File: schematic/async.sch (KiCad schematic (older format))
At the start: 79 parts, among them J1 LOAD, J2 Solar panel, J3 Battery, J4 Screw_Terminal_01x03, J5 Temperature, J6 SD_Micro_5V, J7 Screw_Terminal_01x03, Q1 IRF4905, Q2 IRF4905, Q3 IRF4905, Q4 2N3904, Q5 2N3904, Q6 IRF4905, Q7 2N3904, Q8 IRF4905, Q9 2N3904, SW1 Backlight control, T1 Mains Transformer, U1 ACS712module, U10 ATMEGA328-PU, U2 IR2110, U3 IR2110, U4 DS18B20, U5 ACS712module, U6 DS18B20, U7 DS1307_RTC, U8 MP2307_DC-DC_module, U9 LCDSerial2004

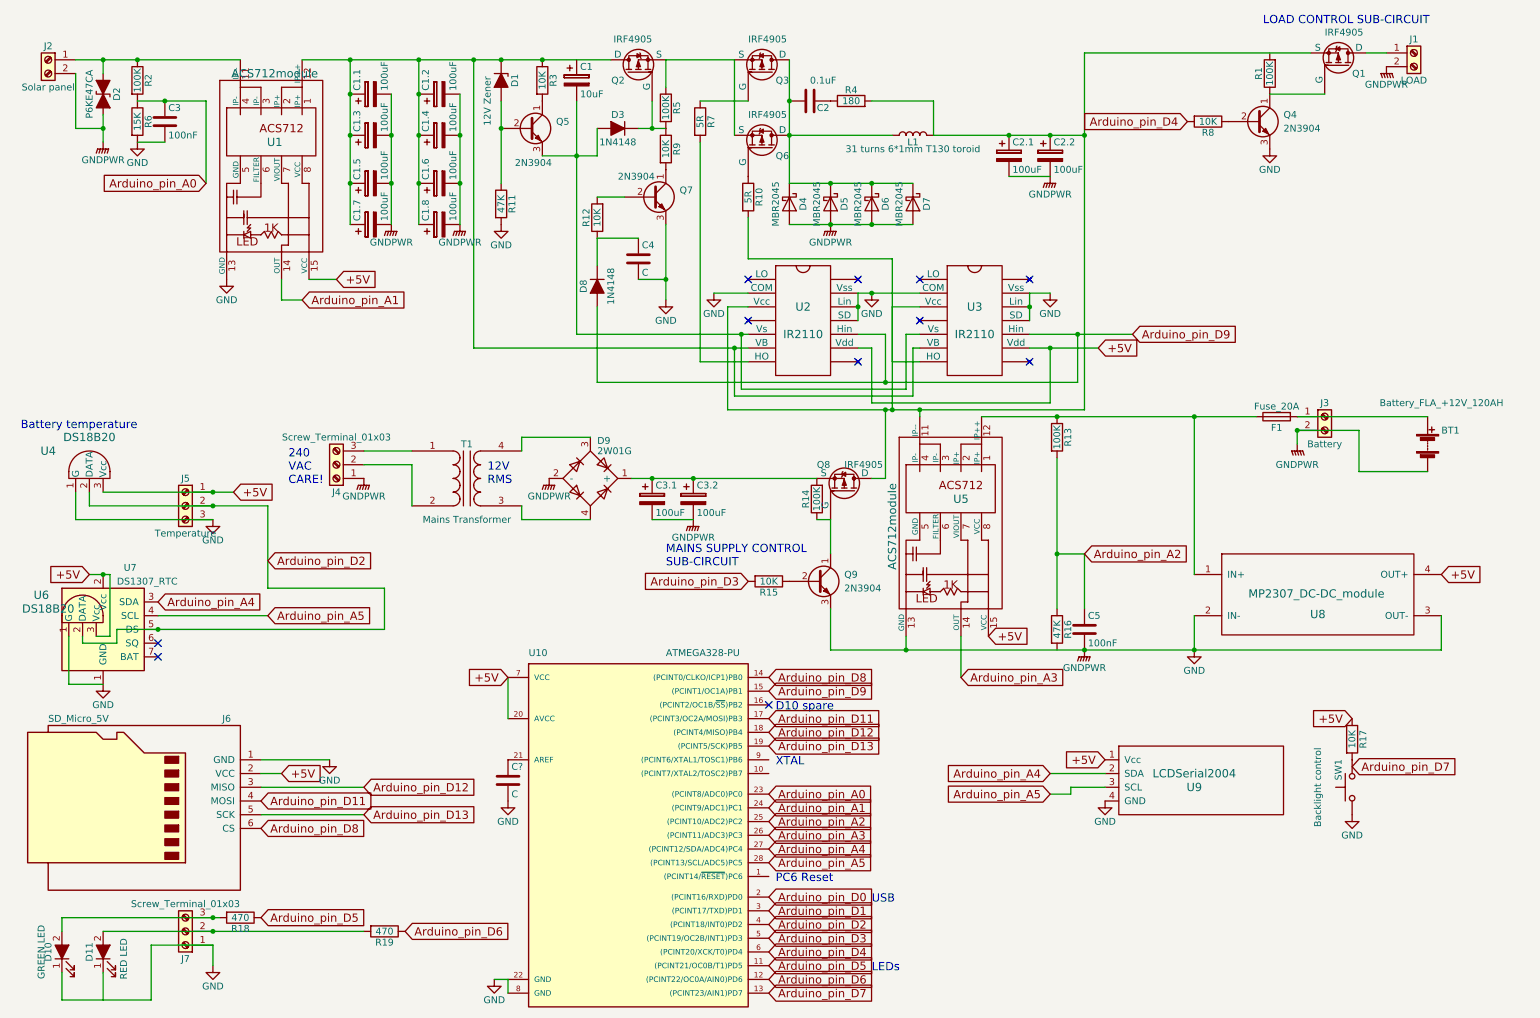
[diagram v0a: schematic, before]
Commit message: added reset button
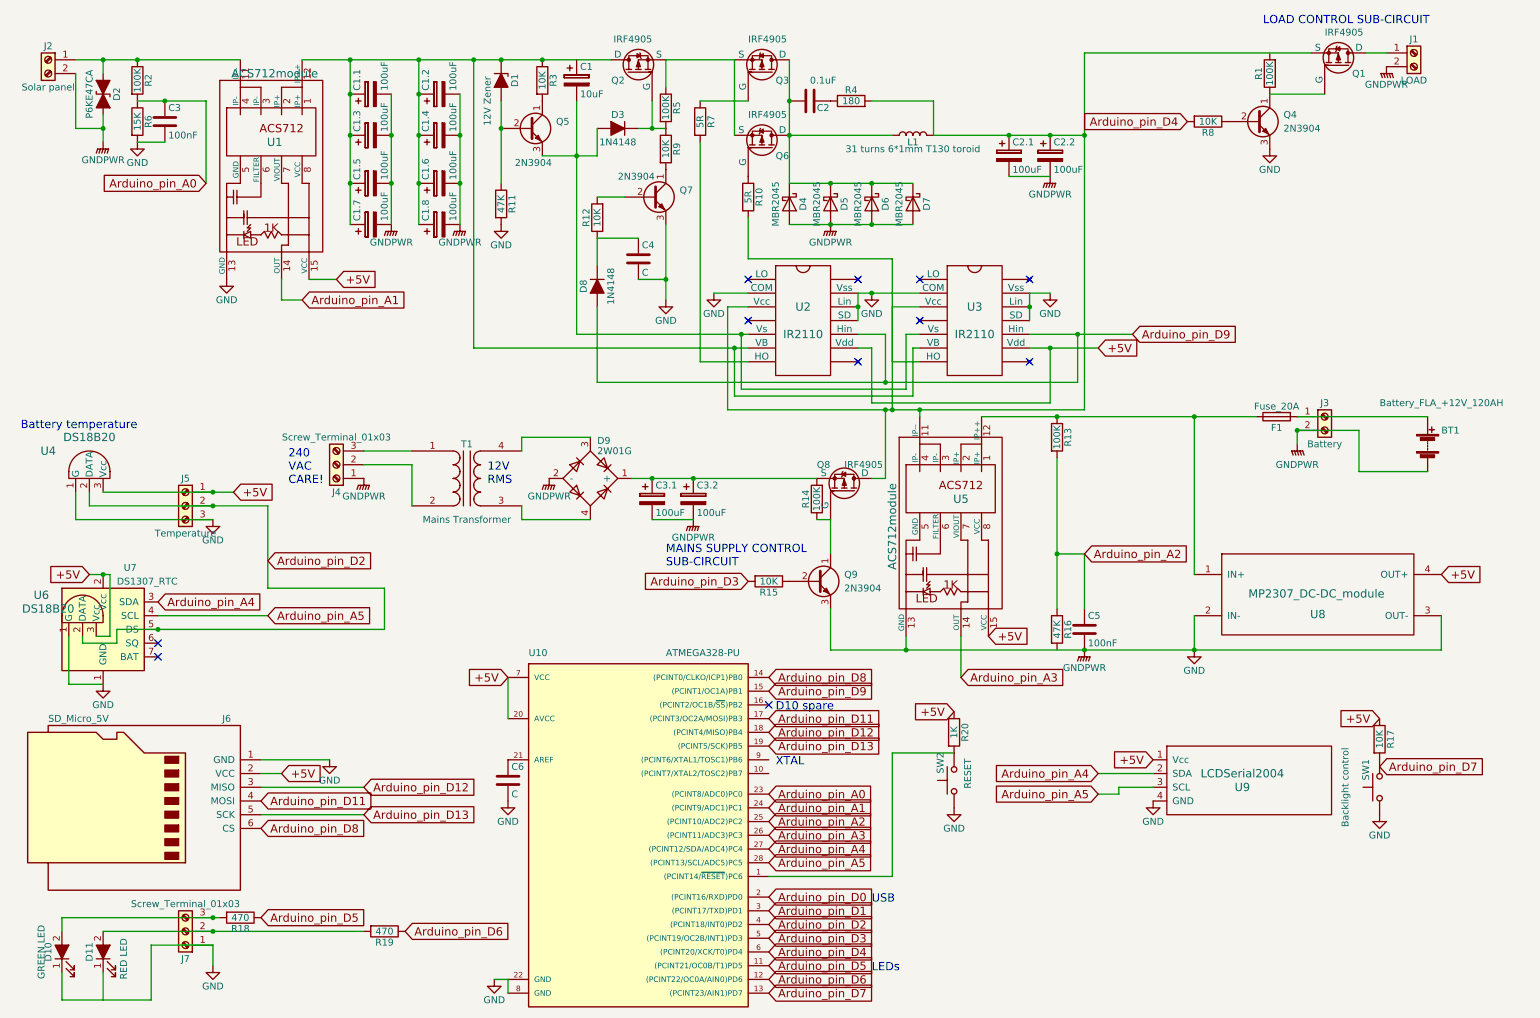
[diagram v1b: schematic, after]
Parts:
- added R20: 1K, symbol R
- added SW2: RESET, symbol SW_Push
- gave numbers to parts that had none: 1
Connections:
- net +5V: now also R20.1
- net GND: now also SW2.1
- net at U10.1 ((PCINT14/~RESET~)PC6): now also R20.2, SW2.2
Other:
- note removed: "PC6 Reset"
- moved on the sheet: R17, SW1, U9
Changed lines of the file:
@@
 L LCDSerial2004 U9
 U 1 1 5AF66609
-P 9050 6150
-F 0 "U9" H 9050 6150 60  0000 C CNN
-F 1 "LCDSerial2004" H 9050 6250 60  0000 C CNN
-F 2 "" H 9050 6150 60  0001 C CNN
-F 3 "" H 9050 6150 60  0001 C CNN
-	1    9050 6150
-	1    0    0    -1
-$EndComp
-Text GLabel 8400 5950 0    60   Input ~ 0
+P 9400 6150
+F 0 "U9" H 9400 6150 60  0000 C CNN
+F 1 "LCDSerial2004" H 9400 6250 60  0000 C CNN
+F 2 "" H 9400 6150 60  0001 C CNN
+F 3 "" H 9400 6150 60  0001 C CNN
+	1    9400 6150
+	1    0    0    -1
+$EndComp
+Text GLabel 8750 5950 0    60   Input ~ 0
 +5V
 $Comp
-L GND #PWR24
+L GND #PWR25
 U 1 1 5AF6660A
-P 8400 6250
-F 0 "#PWR24" H 8400 6000 50  0001 C CNN
-F 1 "GND" H 8400 6100 50  0000 C CNN
-F 2 "" H 8400 6250 50  0001 C CNN
-F 3 "" H 8400 6250 50  0001 C CNN
-	1    8400 6250
-	1    0    0    -1
-$EndComp
-Text GLabel 8000 6050 0    60   Input ~ 0
+P 8750 6250
+F 0 "#PWR25" H 8750 6000 50  0001 C CNN
+F 1 "GND" H 8750 6100 50  0000 C CNN
+F 2 "" H 8750 6250 50  0001 C CNN
+F 3 "" H 8750 6250 50  0001 C CNN
+	1    8750 6250
+	1    0    0    -1
+$EndComp
+Text GLabel 8350 6050 0    60   Input ~ 0
 Arduino_pin_A4
 Wire Wire Line
-	8000 6050 8400 6050
-Text GLabel 8000 6200 0    60   Input ~ 0
+	8350 6050 8750 6050
+Text GLabel 8350 6200 0    60   Input ~ 0
 Arduino_pin_A5
 Wire Wire Line
-	8000 6200 8150 6200
-Wire Wire Line
-	8150 6200 8150 6150
-Wire Wire Line
-	8150 6150 8400 6150
+	8350 6200 8500 6200
+Wire Wire Line
+	8500 6200 8500 6150
+Wire Wire Line
+	8500 6150 8750 6150
 $Comp
 L SW_Push SW1
 U 1 1 5AF6660B
-P 10200 6150
-F 0 "SW1" H 10250 6250 50  0000 L CNN
-F 1 "Backlight control" H 10200 6400 50  0000 C CNN
-F 2 "" H 10200 6350 50  0001 C CNN
-F 3 "" H 10200 6350 50  0001 C CNN
-	1    10200 6150
+P 10400 6150
+F 0 "SW1" H 10450 6250 50  0000 L CNN
+F 1 "Backlight control" H 10400 6400 50  0000 C CNN
+F 2 "" H 10400 6350 50  0001 C CNN
+F 3 "" H 10400 6350 50  0001 C CNN
+	1    10400 6150
 	0    -1   -1   0
 $EndComp
 $Comp
-L GND #PWR25
+L GND #PWR27
 U 1 1 5AF6660C
-P 10200 6350
-F 0 "#PWR25" H 10200 6100 50  0001 C CNN
-F 1 "GND" H 10200 6200 50  0000 C CNN
-F 2 "" H 10200 6350 50  0001 C CNN
-F 3 "" H 10200 6350 50  0001 C CNN
-	1    10200 6350
+P 10400 6350
+F 0 "#PWR27" H 10400 6100 50  0001 C CNN
+F 1 "GND" H 10400 6200 50  0000 C CNN
+F 2 "" H 10400 6350 50  0001 C CNN
+F 3 "" H 10400 6350 50  0001 C CNN
+	1    10400 6350
 	1    0    0    -1
 $EndComp
@@
 L R R17
 U 1 1 5AF6660D
-P 10200 5800
-F 0 "R17" V 10280 5800 50  0000 C CNN
-F 1 "10K" V 10200 5800 50  0000 C CNN
-F 2 "" V 10130 5800 50  0001 C CNN
-F 3 "" H 10200 5800 50  0001 C CNN
-	1    10200 5800
-	1    0    0    -1
-$EndComp
-Text GLabel 10200 5650 0    60   Input ~ 0
+P 10400 5800
+F 0 "R17" V 10480 5800 50  0000 C CNN
+F 1 "10K" V 10400 5800 50  0000 C CNN
+F 2 "" V 10330 5800 50  0001 C CNN
+F 3 "" H 10400 5800 50  0001 C CNN
+	1    10400 5800
+	1    0    0    -1
+$EndComp
+Text GLabel 10400 5650 0    60   Input ~ 0
 +5V
-Text GLabel 10200 6000 2    60   Input ~ 0
+Text GLabel 10400 6000 2    60   Input ~ 0
 Arduino_pin_D7
 Wire Wire Line
@@
 	2300 4700 3150 4700
 Wire Wire Line
-	3150 5000 3150 4700
-Wire Wire Line
-	1200 5000 3150 5000
+	3150 4700 3150 5000
+Wire Wire Line
+	3150 5000 1200 5000
 $Comp
 L DS18B20 U6
@@
 	1050 5050 1150 5050
 Wire Wire Line
-	1150 4600 1150 5050
-Wire Wire Line
-	1000 4600 1150 4600
+	1150 5050 1150 4600
+Wire Wire Line
+	1150 4600 1000 4600
 Wire Wire Line
 	950  5050 950  5100
@@
 	1900 7300 1900 7450
 $Comp
-L GND #PWR26
+L GND #PWR28
 U 1 1 5AF6661E
 P 1900 7450
-F 0 "#PWR26" H 1900 7200 50  0001 C CNN
+F 0 "#PWR28" H 1900 7200 50  0001 C CNN
 F 1 "GND" H 1900 7300 50  0000 C CNN
 F 2 "" H 1900 7450 50  0001 C CNN
@@
 Text Notes 6700 7000 0    60   ~ 0
 USB
-Text Notes 6000 6850 0    60   ~ 0
-PC6 Reset
 Text Notes 6000 6000 0    60   ~ 0
 XTAL
@@
 Connection ~ 1100 4600
 $Comp
-L GND #PWR27
+L GND #PWR29
 U 1 1 5AFFE5F8
 P 3950 7550
-F 0 "#PWR27" H 3950 7300 50  0001 C CNN
+F 0 "#PWR29" H 3950 7300 50  0001 C CNN
 F 1 "GND" H 3950 7400 50  0000 C CNN
 F 2 "" H 3950 7550 50  0001 C CNN
@@
 Arduino_pin_D7
 $Comp
-L C C?
+L C C6
 U 1 1 5B02568E
 P 4050 6100
-F 0 "C?" H 4075 6200 50  0000 L CNN
+F 0 "C6" H 4075 6200 50  0000 L CNN
 F 1 "C" H 4075 6000 50  0000 L CNN
 F 2 "" H 4088 5950 50  0001 C CNN
@@
 $EndComp
 $Comp
-L GND #PWR?
+L GND #PWR24
 U 1 1 5B025790
 P 4050 6250
-F 0 "#PWR?" H 4050 6000 50  0001 C CNN
+F 0 "#PWR24" H 4050 6000 50  0001 C CNN
 F 1 "GND" H 4050 6100 50  0000 C CNN
 F 2 "" H 4050 6250 50  0001 C CNN
@@
 	1    0    0    -1
 $EndComp
+$Comp
+L SW_Push SW2
+U 1 1 5AF7D21C
+P 7300 6100
+F 0 "SW2" H 7350 6200 50  0000 L CNN
+F 1 "RESET" H 7350 6000 50  0000 C CNN
+F 2 "" H 7300 6300 50  0001 C CNN
+F 3 "" H 7300 6300 50  0001 C CNN
+	1    7300 6100
+	0    -1   -1   0
+$EndComp
+$Comp
+L GND #PWR26
+U 1 1 5AF7D222
+P 7300 6300
+F 0 "#PWR26" H 7300 6050 50  0001 C CNN
+F 1 "GND" H 7300 6150 50  0000 C CNN
+F 2 "" H 7300 6300 50  0001 C CNN
+F 3 "" H 7300 6300 50  0001 C CNN
+	1    7300 6300
+	1    0    0    -1
+$EndComp
+$Comp
+L R R20
+U 1 1 5AF7D228
+P 7300 5750
+F 0 "R20" V 7380 5750 50  0000 C CNN
+F 1 "1K" V 7300 5750 50  0000 C CNN
+F 2 "" V 7230 5750 50  0001 C CNN
+F 3 "" H 7300 5750 50  0001 C CNN
+	1    7300 5750
+	1    0    0    -1
+$EndComp
+Text GLabel 7300 5600 0    60   Input ~ 0
++5V
+Wire Wire Line
+	5950 6800 6850 6800
+Wire Wire Line
+	6850 6800 6850 5900
+Wire Wire Line
+	6850 5900 7300 5900
 $EndSCHEMATC

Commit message: added USB B connector
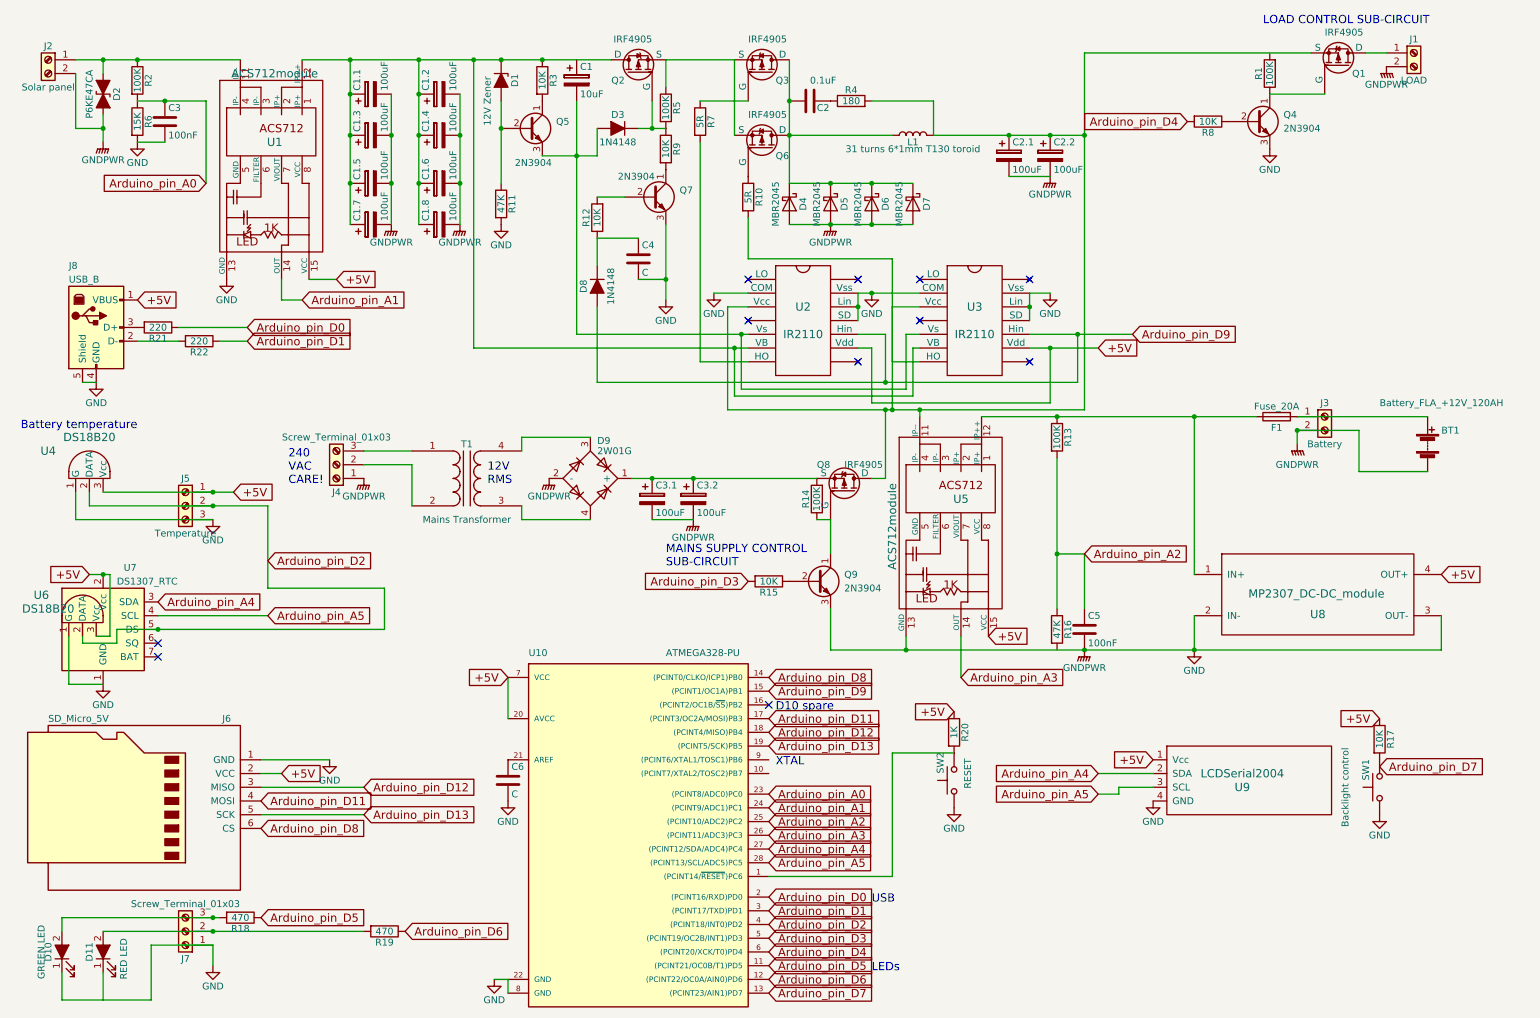
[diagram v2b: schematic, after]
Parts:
- added J8: USB_B, symbol USB_B
- added R21, R22: 220, symbol R
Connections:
- net +5V: now also J8.1 (VBUS)
- net Arduino_pin_D0: now also R21.1
- net Arduino_pin_D1: now also R22.1
- net GND: now also J8.4 (GND), J8.5 (Shield)
- new net: J8.2 (D-), R22.2
- new net: J8.3 (D+), R21.2

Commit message: added BOM and minor component corrections
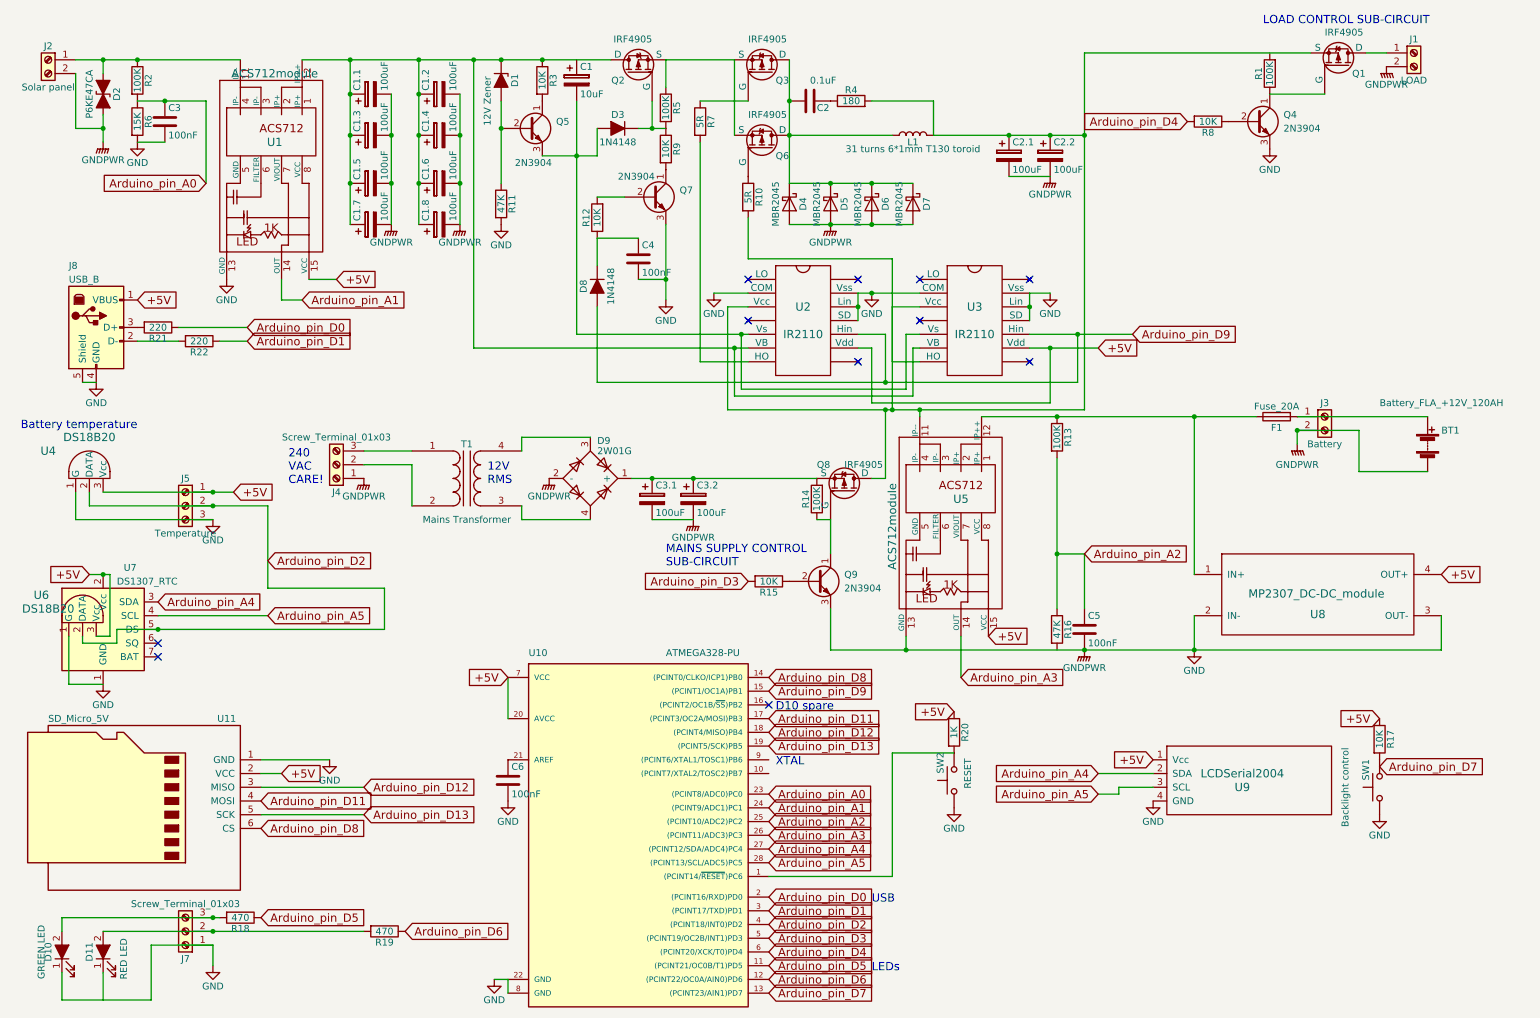
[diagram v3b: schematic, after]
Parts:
- C4, C6: value C -> 100nF
- renumbered J6 to U11
